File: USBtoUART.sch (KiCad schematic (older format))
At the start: 1 part

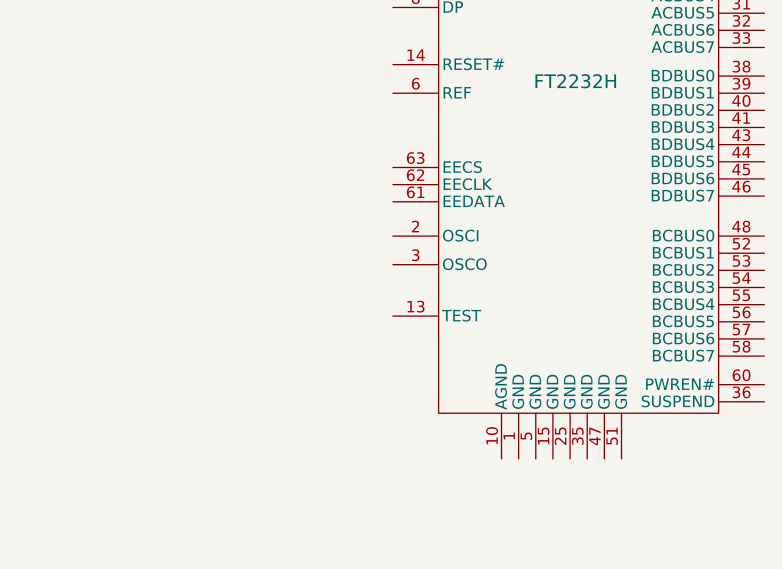
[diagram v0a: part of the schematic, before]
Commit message: working on USB to UART
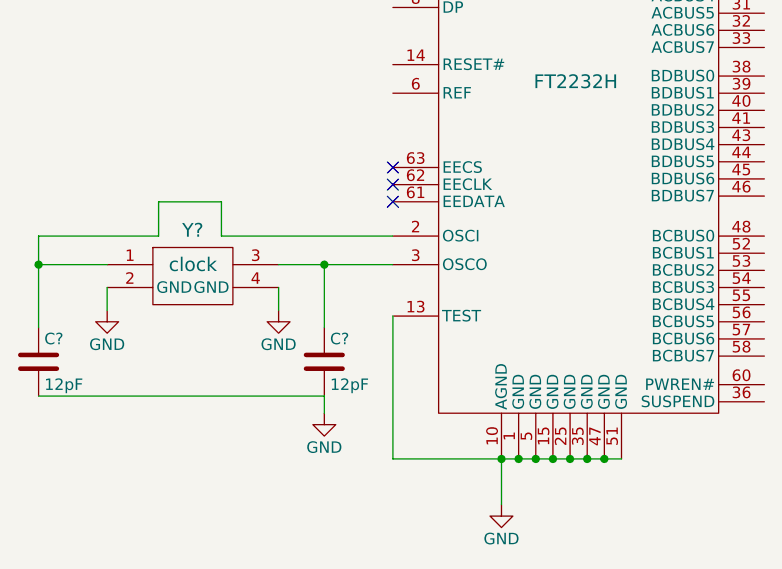
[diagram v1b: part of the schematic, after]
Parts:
- added C? (x2): 12pF, symbol C
- added Y?: clock, symbol clock
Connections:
- net GND: now reaches U?.1 (GND)
- net GND: now also U?.10 (AGND), U?.13 (TEST), U?.15 (GND), U?.25 (GND), U?.35 (GND), U?.47 (GND), U?.5 (GND), U?.51 (GND), C?.2, C?.2, Y?.2 (GND), Y?.4 (GND)
- net at U?.2 (OSCI): now also C?.1, Y?.1
- net at U?.3 (OSCO): now also C?.1, Y?.3
- no-connect marks 0 -> 3
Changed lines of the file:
@@
 	1    0    0    -1
 $EndComp
+$Comp
+L GND #PWR?
+U 1 1 59CD8A85
+P 5175 5325
+F 0 "#PWR?" H 5175 5075 50  0001 C CNN
+F 1 "GND" H 5175 5175 50  0000 C CNN
+F 2 "" H 5175 5325 50  0001 C CNN
+F 3 "" H 5175 5325 50  0001 C CNN
+	1    5175 5325
+	1    0    0    -1
+$EndComp
+$Comp
+L GND #PWR?
+U 1 1 59CD8AF0
+P 4400 4925
+F 0 "#PWR?" H 4400 4675 50  0001 C CNN
+F 1 "GND" H 4400 4775 50  0000 C CNN
+F 2 "" H 4400 4925 50  0001 C CNN
+F 3 "" H 4400 4925 50  0001 C CNN
+	1    4400 4925
+	1    0    0    -1
+$EndComp
+$Comp
+L C C?
+U 1 1 59CD8B05
+P 4400 4700
+F 0 "C?" H 4425 4800 50  0000 L CNN
+F 1 "12pF" H 4425 4600 50  0000 L CNN
+F 2 "" H 4438 4550 50  0001 C CNN
+F 3 "" H 4400 4700 50  0001 C CNN
+	1    4400 4700
+	1    0    0    -1
+$EndComp
+$Comp
+L C C?
+U 1 1 59CD8C67
+P 3150 4700
+F 0 "C?" H 3175 4800 50  0000 L CNN
+F 1 "12pF" H 3175 4600 50  0000 L CNN
+F 2 "" H 3188 4550 50  0001 C CNN
+F 3 "" H 3150 4700 50  0001 C CNN
+	1    3150 4700
+	1    0    0    -1
+$EndComp
+$Comp
+L clock Y?
+U 1 1 59CD8E57
+P 3825 4300
+F 0 "Y?" H 3825 4475 60  0000 C CNN
+F 1 "clock" H 3825 4325 60  0000 C CNN
+F 2 "" H 3825 4300 60  0001 C CNN
+F 3 "" H 3825 4300 60  0001 C CNN
+	1    3825 4300
+	1    0    0    -1
+$EndComp
+$Comp
+L GND #PWR?
+U 1 1 59CD8FB6
+P 4200 4475
+F 0 "#PWR?" H 4200 4225 50  0001 C CNN
+F 1 "GND" H 4200 4325 50  0000 C CNN
+F 2 "" H 4200 4475 50  0001 C CNN
+F 3 "" H 4200 4475 50  0001 C CNN
+	1    4200 4475
+	1    0    0    -1
+$EndComp
+$Comp
+L GND #PWR?
+U 1 1 59CD8FE5
+P 3450 4475
+F 0 "#PWR?" H 3450 4225 50  0001 C CNN
+F 1 "GND" H 3450 4325 50  0000 C CNN
+F 2 "" H 3450 4475 50  0001 C CNN
+F 3 "" H 3450 4475 50  0001 C CNN
+	1    3450 4475
+	1    0    0    -1
+$EndComp
+Wire Wire Line
+	4700 4500 4700 5125
+Wire Wire Line
+	4700 5125 5700 5125
+Wire Wire Line
+	5175 5125 5175 5325
+Connection ~ 5625 5125
+Connection ~ 5550 5125
+Connection ~ 5475 5125
+Connection ~ 5400 5125
+Connection ~ 5325 5125
+Connection ~ 5175 5125
+Connection ~ 5250 5125
+Wire Wire Line
+	3450 4375 3450 4475
+Wire Wire Line
+	4200 4375 4200 4475
+Wire Wire Line
+	4700 4275 4200 4275
+Wire Wire Line
+	4400 4275 4400 4550
+Connection ~ 4400 4275
+Wire Wire Line
+	3450 4275 3150 4275
+Wire Wire Line
+	3150 4150 3150 4550
+Wire Wire Line
+	3150 4850 4400 4850
+Wire Wire Line
+	4400 4850 4400 4925
+Wire Wire Line
+	4700 4150 3950 4150
+Wire Wire Line
+	3950 4150 3950 4000
+Wire Wire Line
+	3950 4000 3675 4000
+Wire Wire Line
+	3675 4000 3675 4150
+Wire Wire Line
+	3675 4150 3150 4150
+Connection ~ 3150 4275
+NoConn ~ 4700 4000
+NoConn ~ 4700 3925
+NoConn ~ 4700 3850
 $EndSCHEMATC

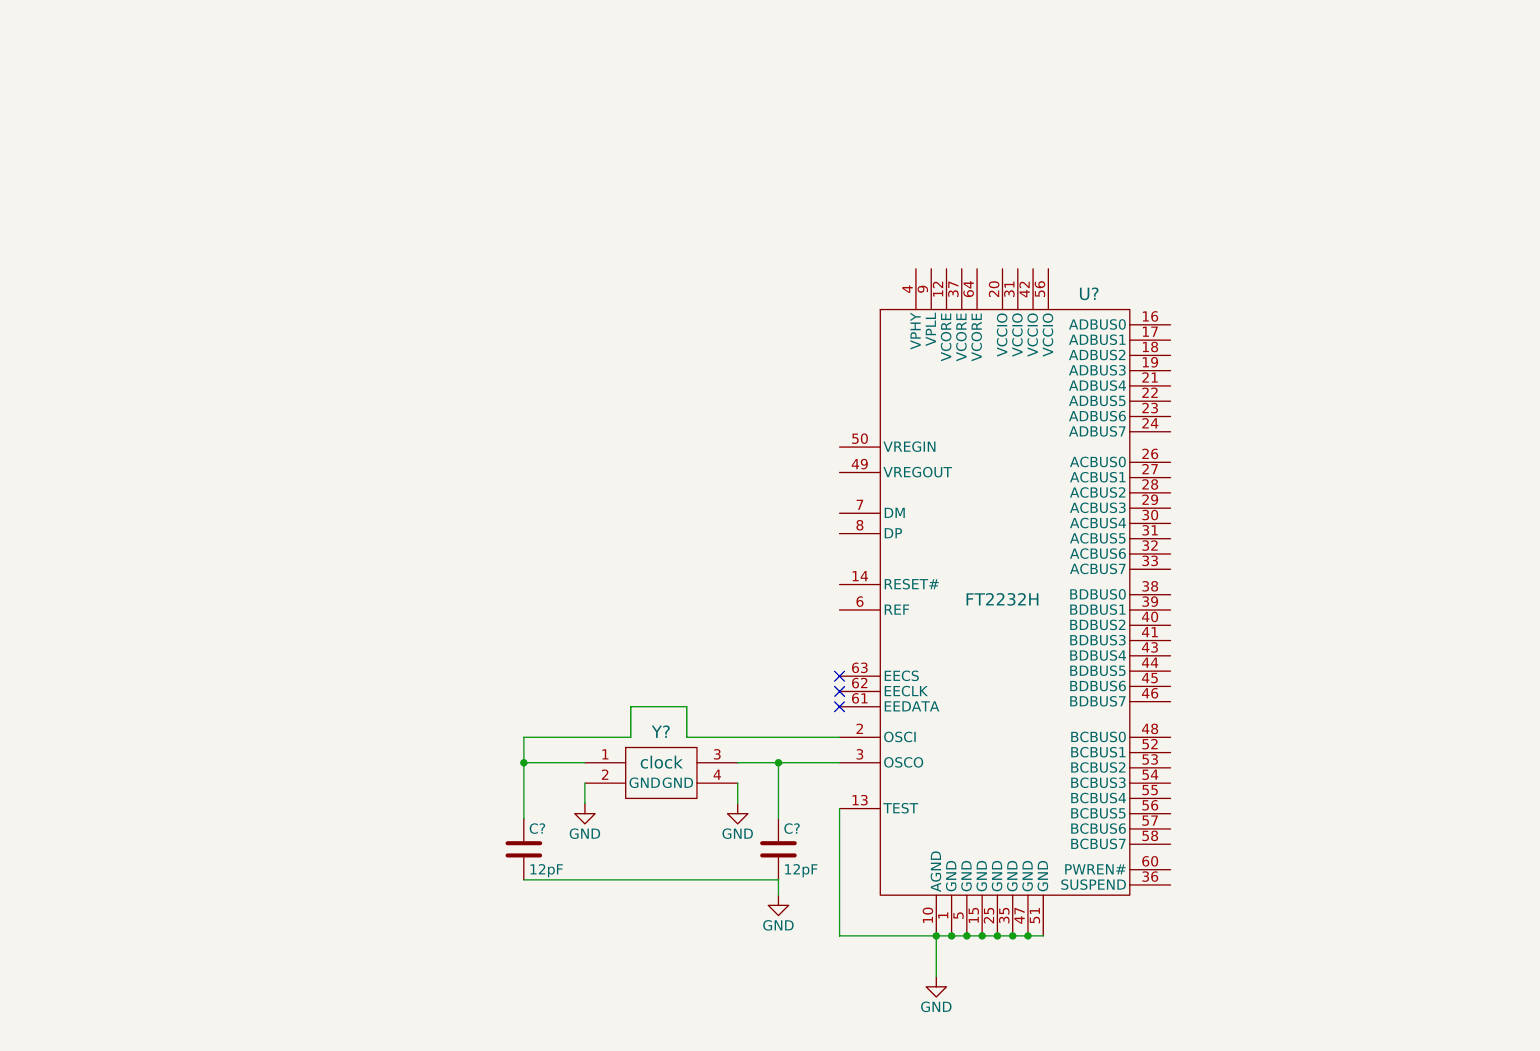
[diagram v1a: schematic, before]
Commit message: finsihed USB to UART shcematic
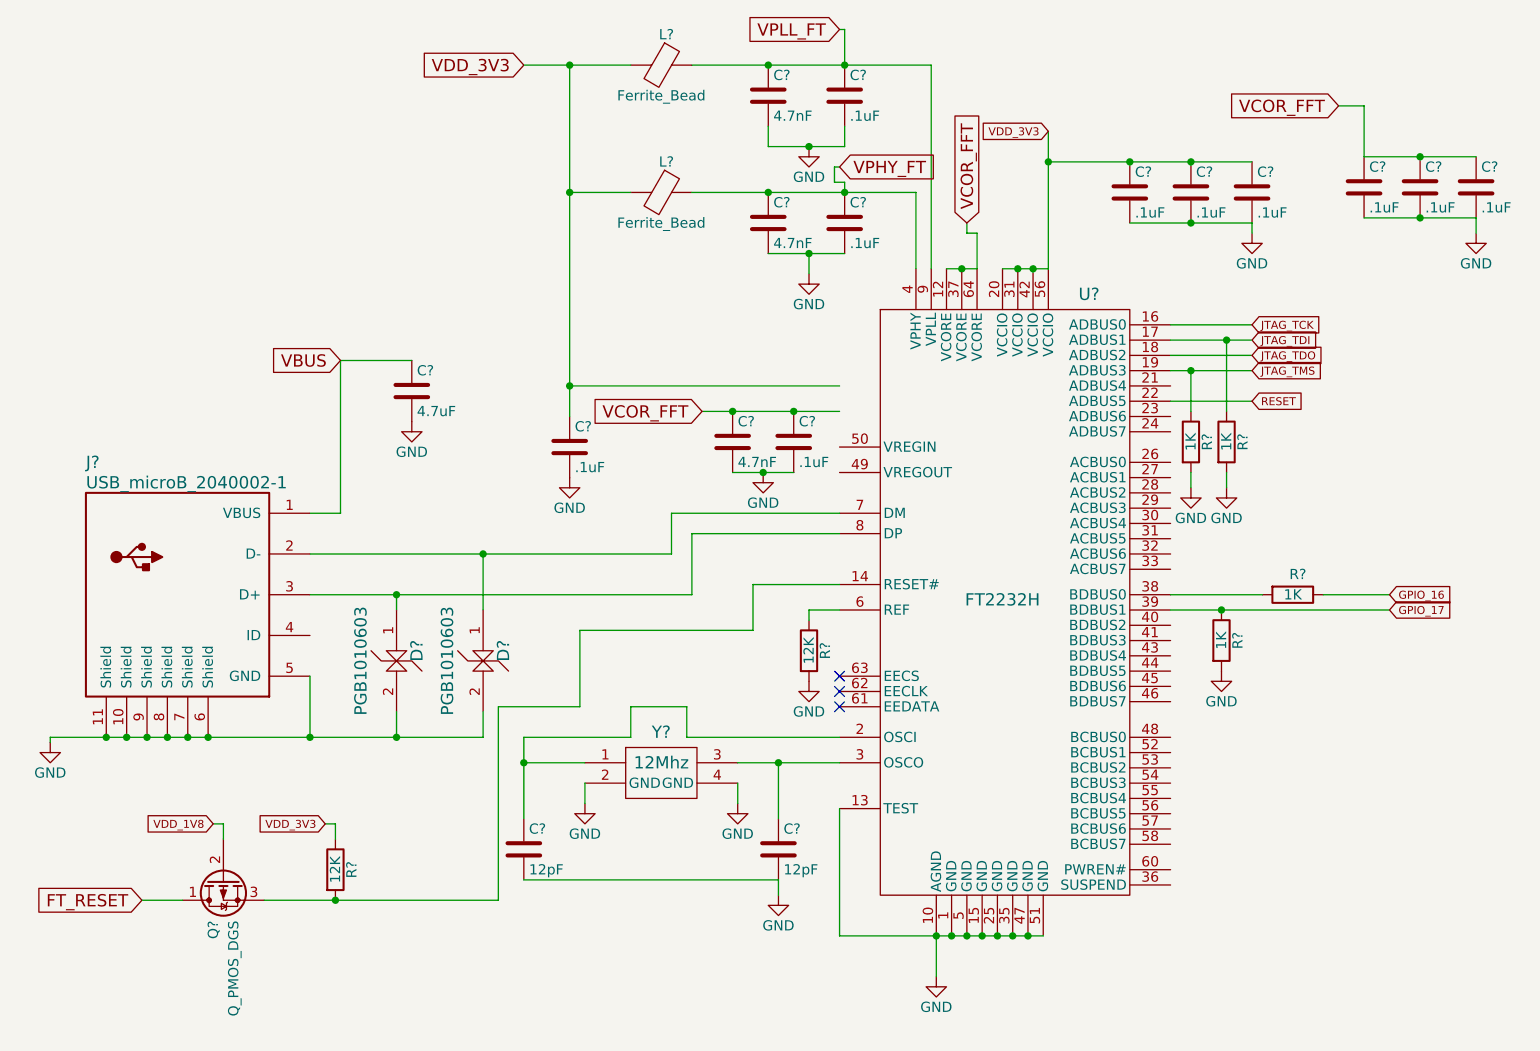
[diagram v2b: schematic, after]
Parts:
- added C? (x3): 4.7nF, symbol C
- added C? (x10): .1uF, symbol C
- added C?: 4.7uF, symbol C
- added D? (x2): PGB1010603, symbol PGB1010603
- added J?: USB_microB_2040002-1, symbol USB_microB_2040002-1
- added L? (x2): Ferrite_Bead, symbol Ferrite_Bead
- added Q?: Q_PMOS_DGS, symbol Q_PMOS_DGS
- added R? (x2): 12K, symbol R
- added R? (x4): 1K, symbol R
- Y?: value clock -> 12Mhz
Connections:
- net GND: now also C?.2, C?.2, C?.2, C?.2, C?.2, C?.2, C?.2, C?.2, C?.2, C?.2, C?.2, C?.2, C?.2, C?.2, D?.2, D?.2, J?.10 (Shield), J?.11 (Shield), J?.5 (GND), J?.6 (Shield), J?.7 (Shield), J?.8 (Shield), J?.9 (Shield), R?.2, R?.2, R?.2, R?.2
- net VCOR_FFT: now reaches U?.12 (VCORE)
- net VCOR_FFT: now also U?.37 (VCORE), U?.64 (VCORE), C?.1, C?.1, C?.1, C?.1, C?.1
- net at U?.14 (RESET#): now also Q?.3 (S), R?.2
- net JTAG_TCK: now reaches U?.16 (ADBUS0)
- net JTAG_TDI: now reaches U?.17 (ADBUS1)
- net JTAG_TDI: now also R?.1
- net JTAG_TDO: now reaches U?.18 (ADBUS2)
- net JTAG_TMS: now reaches U?.19 (ADBUS3)
- net JTAG_TMS: now also R?.1
- net VDD_3V3: now reaches U?.20 (VCCIO)
- net VDD_3V3: now also U?.31 (VCCIO), U?.42 (VCCIO), U?.56 (VCCIO), C?.1, C?.1, C?.1, C?.1, L?.2, L?.2, R?.1
- net RESET: now reaches U?.22 (ADBUS5)
- net at U?.38 (BDBUS0): now also R?.2
- net GPIO_17: now reaches U?.39 (BDBUS1)
- net GPIO_17: now also R?.1
- net VPHY_FT: now reaches U?.4 (VPHY)
- net VPHY_FT: now also C?.1, C?.1, L?.1
- net at U?.6 (REF): now also R?.1
- net at U?.7 (DM): now also D?.1, J?.2 (D-)
- net at U?.8 (DP): now also D?.1, J?.3 (D+)
- net VPLL_FT: now reaches U?.9 (VPLL)
- net VPLL_FT: now also C?.1, C?.1, L?.1
- new net FT_RESET: Q?.1 (D)
- new net GPIO_16: R?.1
- new net VBUS: C?.1, J?.1 (VBUS)
- new net VDD_1V8: Q?.2 (G)

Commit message: update
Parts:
- removed C? (x3): 4.7nF, symbol C
- removed C? (x10): .1uF, symbol C
- removed C?: 4.7uF, symbol C
- removed D? (x2): PGB1010603, symbol PGB1010603
- removed J?: USB_microB_2040002-1, symbol USB_microB_2040002-1
- removed L? (x2): Ferrite_Bead, symbol Ferrite_Bead
- removed Q?: Q_PMOS_DGS, symbol Q_PMOS_DGS
- removed R? (x2): 12K, symbol R
- removed R? (x4): 1K, symbol R
- Y?: value 12Mhz -> clock
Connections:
- net GPIO_17: no longer names the net of U?.39 (BDBUS1)
- net JTAG_TCK: no longer names the net of U?.16 (ADBUS0)
- net JTAG_TDI: no longer names the net of U?.17 (ADBUS1)
- net JTAG_TDO: no longer names the net of U?.18 (ADBUS2)
- net JTAG_TMS: no longer names the net of U?.19 (ADBUS3)
- net RESET: no longer names the net of U?.22 (ADBUS5)
- removed net VCOR_FFT: U?.12 (VCORE), U?.37 (VCORE), U?.64 (VCORE)
- removed net VDD_3V3: U?.20 (VCCIO), U?.31 (VCCIO), U?.42 (VCCIO), U?.56 (VCCIO)
- net VPHY_FT: no longer names the net of U?.4 (VPHY)
- net VPLL_FT: no longer names the net of U?.9 (VPLL)

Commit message: fixing deleted USBtoUART
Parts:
- added C? (x3): 4.7nF, symbol C
- added C? (x10): .1uF, symbol C
- added C?: 4.7uF, symbol C
- added D? (x2): PGB1010603, symbol PGB1010603
- added J?: USB_microB_2040002-1, symbol USB_microB_2040002-1
- added L? (x2): Ferrite_Bead, symbol Ferrite_Bead
- added Q?: Q_PMOS_DGS, symbol Q_PMOS_DGS
- added R? (x2): 12K, symbol R
- added R? (x4): 1K, symbol R
- Y?: value clock -> 12Mhz
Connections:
- net GND: now also C?.2, C?.2, C?.2, C?.2, C?.2, C?.2, C?.2, C?.2, C?.2, C?.2, C?.2, C?.2, C?.2, C?.2, D?.2, D?.2, J?.10 (Shield), J?.11 (Shield), J?.5 (GND), J?.6 (Shield), J?.7 (Shield), J?.8 (Shield), J?.9 (Shield), R?.2, R?.2, R?.2, R?.2
- net VCOR_FFT: now reaches U?.12 (VCORE)
- net VCOR_FFT: now also U?.37 (VCORE), U?.64 (VCORE), C?.1, C?.1, C?.1, C?.1, C?.1
- net at U?.14 (RESET#): now also Q?.3 (S), R?.2
- net JTAG_TCK: now reaches U?.16 (ADBUS0)
- net JTAG_TDI: now reaches U?.17 (ADBUS1)
- net JTAG_TDI: now also R?.1
- net JTAG_TDO: now reaches U?.18 (ADBUS2)
- net JTAG_TMS: now reaches U?.19 (ADBUS3)
- net JTAG_TMS: now also R?.1
- net VDD_3V3: now reaches U?.20 (VCCIO)
- net VDD_3V3: now also U?.31 (VCCIO), U?.42 (VCCIO), U?.56 (VCCIO), C?.1, C?.1, C?.1, C?.1, L?.2, L?.2, R?.1
- net RESET: now reaches U?.22 (ADBUS5)
- net at U?.38 (BDBUS0): now also R?.2
- net GPIO_17: now reaches U?.39 (BDBUS1)
- net GPIO_17: now also R?.1
- net VPHY_FT: now reaches U?.4 (VPHY)
- net VPHY_FT: now also C?.1, C?.1, L?.1
- net at U?.6 (REF): now also R?.1
- net at U?.7 (DM): now also D?.1, J?.2 (D-)
- net at U?.8 (DP): now also D?.1, J?.3 (D+)
- net VPLL_FT: now reaches U?.9 (VPLL)
- net VPLL_FT: now also C?.1, C?.1, L?.1
- new net FT_RESET: Q?.1 (D)
- new net GPIO_16: R?.1
- new net VBUS: C?.1, J?.1 (VBUS)
- new net VDD_1V8: Q?.2 (G)
